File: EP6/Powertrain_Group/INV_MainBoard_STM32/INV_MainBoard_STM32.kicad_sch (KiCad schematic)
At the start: 17 parts, among them J1 FX26-30P-1SV, J10 current_DC, J2 motorSense, J9 CAN

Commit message: Inverter board adjust
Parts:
- R4: footprint Resistor_SMD:R_0402_1005Metric -> Resistor_SMD:R_0603_1608Metric
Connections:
- net GND: no longer J1.MP1, J1.MP2, J1.MP3, J1.MP4
- no-connect marks 0 -> 4
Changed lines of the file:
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@@
 	)
 	(junction
-		(at 48.26 130.81)
-		(diameter 0)
-		(color 0 0 0 0)
-	)
-	(junction
-		(at 49.53 185.42)
-		(diameter 0)
-		(color 0 0 0 0)
-	)
-	(junction
 		(at 67.31 149.86)
 		(diameter 0)
@@
 		(color 0 0 0 0)
 	)
+	(no_connect
+		(at 48.26 134.62)
+	)
+	(no_connect
+		(at 50.8 185.42)
+	)
+	(no_connect
+		(at 50.8 134.62)
+	)
+	(no_connect
+		(at 48.26 185.42)
+	)
 	(wire
 		(pts
@@
 	(wire
 		(pts
-			(xy 50.8 134.62) (xy 50.8 130.81)
-		)
-		(stroke
-			(width 0)
-			(type default)
-		)
-	)
-	(wire
-		(pts
 			(xy 31.75 157.48) (xy 35.56 157.48)
 		)
@@
 	(wire
 		(pts
-			(xy 49.53 185.42) (xy 50.8 185.42)
-		)
-		(stroke
-			(width 0)
-			(type default)
-		)
-	)
-	(wire
-		(pts
 			(xy 63.5 144.78) (xy 67.31 144.78)
 		)
@@
 	(wire
 		(pts
-			(xy 50.8 130.81) (xy 48.26 130.81)
-		)
-		(stroke
-			(width 0)
-			(type default)
-		)
-	)
-	(wire
-		(pts
 			(xy 154.94 38.1) (xy 151.13 38.1)
 		)
@@
 	(wire
 		(pts
-			(xy 49.53 187.96) (xy 49.53 185.42)
-		)
-		(stroke
-			(width 0)
-			(type default)
-		)
-	)
-	(wire
-		(pts
 			(xy 69.85 142.24) (xy 63.5 142.24)
 		)
@@
 	(wire
 		(pts
-			(xy 44.45 130.81) (xy 48.26 130.81)
-		)
-		(stroke
-			(width 0)
-			(type default)
-		)
-	)
-	(wire
-		(pts
 			(xy 64.77 152.4) (xy 64.77 154.94)
 		)
@@
 	(wire
 		(pts
-			(xy 48.26 130.81) (xy 48.26 134.62)
-		)
-		(stroke
-			(width 0)
-			(type default)
-		)
-	)
-	(wire
-		(pts
 			(xy 142.24 138.43) (xy 137.16 138.43)
 		)
@@
 	(wire
 		(pts
-			(xy 48.26 185.42) (xy 49.53 185.42)
-		)
-		(stroke
-			(width 0)
-			(type default)
-		)
-	)
-	(wire
-		(pts
 			(xy 31.75 144.78) (xy 31.75 149.86)
 		)
@@
 	(symbol
 		(lib_id "power:GND")
-		(at 44.45 130.81 0)
-		(unit 1)
-		(exclude_from_sim no)
-		(in_bom yes)
-		(on_board yes)
-		(dnp no)
-		(fields_autoplaced yes)
-		(property "Reference" "#PWR04"
-			(at 44.45 137.16 0)
-			(effects
-				(font
-					(size 1.27 1.27)
-				)
-				(hide yes)
-			)
-		)
-		(property "Value" "GND"
-			(at 44.45 135.89 0)
-			(effects
-				(font
-					(size 1.27 1.27)
-				)
-				(hide yes)
-			)
-		)
-		(property "Footprint" ""
-			(at 44.45 130.81 0)
-			(effects
-				(font
-					(size 1.27 1.27)
-				)
-				(hide yes)
-			)
-		)
-		(property "Datasheet" ""
-			(at 44.45 130.81 0)
-			(effects
-				(font
-					(size 1.27 1.27)
-				)
-				(hide yes)
-			)
-		)
-		(property "Description" "Power symbol creates a global label with name \"GND\" , ground"
-			(at 44.45 130.81 0)
-			(effects
-				(font
-					(size 1.27 1.27)
-				)
-				(hide yes)
-			)
-		)
-		(pin "1"
-		)
-		(instances
-			(project "INV_MainBoard_STM32"
-				(path "/963ad98e-e494-4953-a7e0-8b20a365a35d"
-					(reference "#PWR04")
-					(unit 1)
-				)
-			)
-		)
-	)
-	(symbol
-		(lib_id "power:GND")
 		(at 20.32 157.48 0)
 		(unit 1)
@@
 			)
 		)
-		(property "Footprint" "Resistor_SMD:R_0402_1005Metric"
+		(property "Footprint" "Resistor_SMD:R_0603_1608Metric"
 			(at 196.85 142.24 0)
 			(effects
@@
 					(unit 1)
 				)
-			)
-		)
-	)
-	(symbol
-		(lib_id "power:GND")
-		(at 49.53 187.96 0)
-		(unit 1)
-		(exclude_from_sim no)
-		(in_bom yes)
-		(on_board yes)
-		(dnp no)
-		(fields_autoplaced yes)
-		(property "Reference" "#PWR019"
-			(at 49.53 194.31 0)
-			(effects
-				(font
-					(size 1.27 1.27)
-				)
-				(hide yes)
-			)
-		)
-		(property "Value" "GND"
-			(at 49.53 193.04 0)
-			(effects
-				(font
-					(size 1.27 1.27)
-				)
-				(hide yes)
-			)
-		)
-		(property "Footprint" ""
-			(at 49.53 187.96 0)
-			(effects
-				(font
-					(size 1.27 1.27)
-				)
-				(hide yes)
-			)
-		)
-		(property "Datasheet" ""
-			(at 49.53 187.96 0)
-			(effects
-				(font
-					(size 1.27 1.27)
-				)
-				(hide yes)
-			)
-		)
-		(property "Description" "Power symbol creates a global label with name \"GND\" , ground"
-			(at 49.53 187.96 0)
-			(effects
-				(font
-					(size 1.27 1.27)
-				)
-				(hide yes)
-			)
-		)
-		(pin "1"
-		)
-		(instances
-			(project "INV_MainBoard_STM32"
-				(path "/963ad98e-e494-4953-a7e0-8b20a365a35d"
-					(reference "#PWR019")
-					(unit 1)
-				)

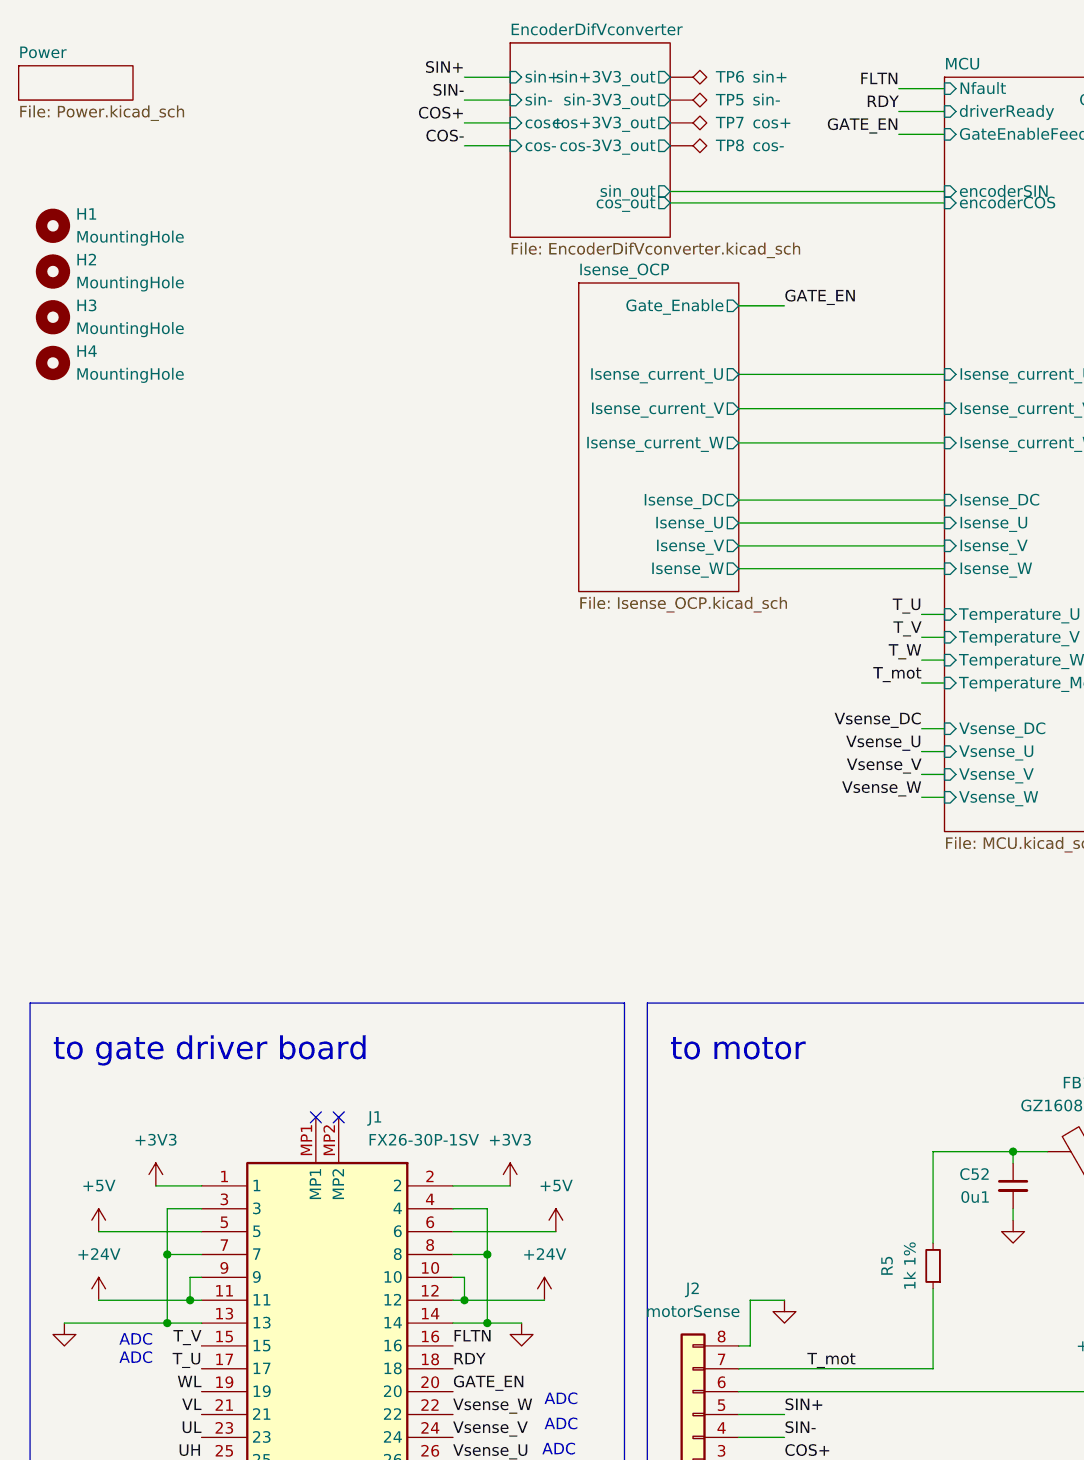
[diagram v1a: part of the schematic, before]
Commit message: batch update for JLCPCB 241117
6SBMS
ACC_HVLV1
INV_CurrentSense2
INV_CurrentSense3
DClinkCap1
INV_MainBoard_STM32
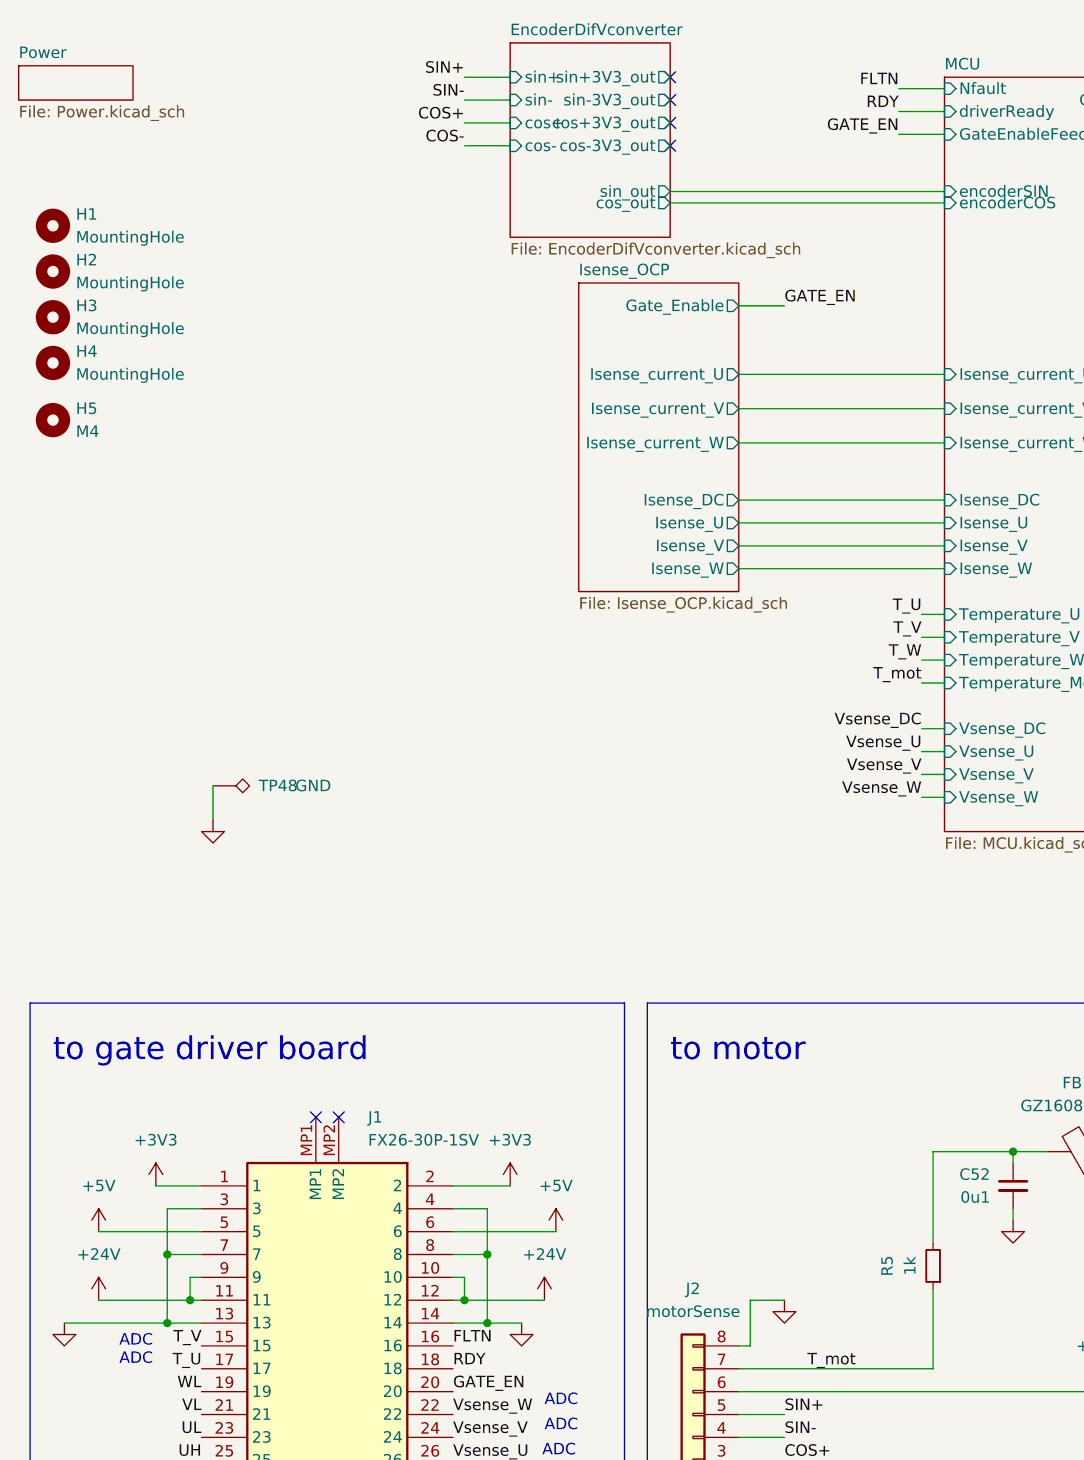
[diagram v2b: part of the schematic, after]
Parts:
- removed TP5: sin-, TestPoint:TestPoint_THTPad_D1.0mm_Drill0.5mm, symbol Connector:TestPoint_Alt
- removed TP6: sin+, TestPoint:TestPoint_THTPad_D1.0mm_Drill0.5mm, symbol Connector:TestPoint_Alt
- removed TP7: cos+, TestPoint:TestPoint_THTPad_D1.0mm_Drill0.5mm, symbol Connector:TestPoint_Alt
- removed TP8: cos-, TestPoint:TestPoint_THTPad_D1.0mm_Drill0.5mm, symbol Connector:TestPoint_Alt
- added H5: M4, MountingHole:MountingHole_4mm, symbol Mechanical:MountingHole
- added TP48: GND, TestPoint:TestPoint_THTPad_D1.0mm_Drill0.5mm, symbol Connector:TestPoint_Alt
- R5: value 1k 1% -> 1k
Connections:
- net GND: now also TP48.1
- no-connect marks 4 -> 8
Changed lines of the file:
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@@
 	(title_block
 		(title "INV_MainBoard")
-		(date "2024-11-15")
-		(rev "1")
+		(date "2024-11-16")
+		(rev "1.0")
 		(company "NTURacing Team")
 		(comment 1 "郭哲明 Jack Kuo")
@@
 	)
 	(no_connect
+		(at 87.63 26.67)
+	)
+	(no_connect
+		(at 87.63 19.05)
+	)
+	(no_connect
+		(at 87.63 24.13)
+	)
+	(no_connect
 		(at 48.26 134.62)
 	)
@@
 	)
 	(no_connect
+		(at 87.63 21.59)
+	)
+	(no_connect
 		(at 48.26 185.42)
 	)
@@
 	(wire
 		(pts
+			(xy 36.83 97.79) (xy 36.83 101.6)
+		)
+		(stroke
+			(width 0)
+			(type default)
+		)
+	)
+	(wire
+		(pts
 			(xy 115.57 86.36) (xy 118.11 86.36)
 		)
@@
 	)
 	(symbol
-		(lib_id "Connector:TestPoint_Alt")
-		(at 87.63 21.59 270)
-		(unit 1)
-		(exclude_from_sim no)
-		(in_bom yes)
-		(on_board yes)
-		(dnp no)
-		(property "Reference" "TP5"
-			(at 92.71 21.59 90)
-			(effects
-				(font
-					(size 1.27 1.27)
-				)
-				(justify left)
-			)
-		)
-		(property "Value" "sin-"
-			(at 96.774 21.59 90)
-			(effects
-				(font
-					(size 1.27 1.27)
-				)
-				(justify left)
-			)
-		)
-		(property "Footprint" "TestPoint:TestPoint_THTPad_D1.0mm_Drill0.5mm"
-			(at 87.63 26.67 0)
-			(effects
-				(font
-					(size 1.27 1.27)
-				)
-				(hide yes)
-			)
-		)
-		(property "Datasheet" "~"
-			(at 87.63 26.67 0)
-			(effects
-				(font
-					(size 1.27 1.27)
-				)
-				(hide yes)
-			)
-		)
-		(property "Description" "test point (alternative shape)"
-			(at 87.63 21.59 0)
-			(effects
-				(font
-					(size 1.27 1.27)
-				)
-				(hide yes)
-			)
-		)
-		(pin "1"
-		)
-		(instances
-			(project ""
-				(path "/963ad98e-e494-4953-a7e0-8b20a365a35d"
-					(reference "TP5")
-					(unit 1)
-				)
-			)
-		)
-	)
-	(symbol
 		(lib_id "power:+5V")
 		(at 24.13 147.32 0)
@@
 	)
 	(symbol
-		(lib_id "Connector:TestPoint_Alt")
-		(at 87.63 24.13 270)
+		(lib_id "Device:R_Small")
+		(at 116.84 151.13 180)
 		(unit 1)
 		(exclude_from_sim no)
@@
 		(on_board yes)
 		(dnp no)
-		(property "Reference" "TP7"
-			(at 92.71 24.13 90)
+		(property "Reference" "R5"
+			(at 111.76 151.13 90)
 			(effects
 				(font
 					(size 1.27 1.27)
 				)
-				(justify left)
 			)
 		)
-		(property "Value" "cos+"
-			(at 96.774 24.13 90)
+		(property "Value" "1k"
+			(at 114.3 151.13 90)
 			(effects
 				(font
 					(size 1.27 1.27)
 				)
-				(justify left)
 			)
 		)
-		(property "Footprint" "TestPoint:TestPoint_THTPad_D1.0mm_Drill0.5mm"
-			(at 87.63 29.21 0)
+		(property "Footprint" "Resistor_SMD:R_0603_1608Metric"
+			(at 116.84 151.13 0)
 			(effects
 				(font
@@
 		)
 		(property "Datasheet" "~"
-			(at 87.63 29.21 0)
+			(at 116.84 151.13 0)
 			(effects
 				(font
@@
 			)
 		)
-		(property "Description" "test point (alternative shape)"
-			(at 87.63 24.13 0)
+		(property "Description" "Resistor, small symbol"
+			(at 116.84 151.13 0)
 			(effects
 				(font
@@
 			)
 		)
+		(pin "2"
+		)
 		(pin "1"
 		)
@@
 			(project "INV_MainBoard_STM32"
 				(path "/963ad98e-e494-4953-a7e0-8b20a365a35d"
-					(reference "TP7")
+					(reference "R5")
 					(unit 1)
 				)
@@
 	)
 	(symbol
-		(lib_id "Device:R_Small")
-		(at 116.84 151.13 180)
+		(lib_id "Mechanical:MountingHole")
+		(at 19.05 57.15 0)
 		(unit 1)
-		(exclude_from_sim no)
-		(in_bom yes)
+		(exclude_from_sim yes)
+		(in_bom no)
 		(on_board yes)
 		(dnp no)
-		(property "Reference" "R5"
-			(at 111.76 151.13 90)
+		(fields_autoplaced yes)
+		(property "Reference" "H5"
+			(at 21.59 55.88 0)
 			(effects
 				(font
 					(size 1.27 1.27)
 				)
+				(justify left)
 			)
 		)
-		(property "Value" "1k 1%"
-			(at 114.3 151.13 90)
+		(property "Value" "M4"
+			(at 21.59 58.42 0)
 			(effects
 				(font
 					(size 1.27 1.27)
 				)
+				(justify left)
 			)
 		)
-		(property "Footprint" "Resistor_SMD:R_0603_1608Metric"
-			(at 116.84 151.13 0)
+		(property "Footprint" "MountingHole:MountingHole_4mm"
+			(at 19.05 57.15 0)
 			(effects
 				(font
@@
 		)
 		(property "Datasheet" "~"
-			(at 116.84 151.13 0)
+			(at 19.05 57.15 0)
 			(effects
 				(font
@@
 			)
 		)
-		(property "Description" "Resistor, small symbol"
-			(at 116.84 151.13 0)
+		(property "Description" "Mounting Hole without connection"
+			(at 19.05 57.15 0)
 			(effects
 				(font
@@
 			)
 		)
-		(pin "2"
-		)
-		(pin "1"
-		)
 		(instances
 			(project "INV_MainBoard_STM32"
 				(path "/963ad98e-e494-4953-a7e0-8b20a365a35d"
-					(reference "R5")
+					(reference "H5")
 					(unit 1)
 				)
@@
 	)
 	(symbol
+		(lib_id "Connector:TestPoint_Alt")
+		(at 36.83 97.79 270)
+		(unit 1)
+		(exclude_from_sim no)
+		(in_bom yes)
+		(on_board yes)
+		(dnp no)
+		(property "Reference" "TP48"
+			(at 41.91 97.79 90)
+			(effects
+				(font
+					(size 1.27 1.27)
+				)
+				(justify left)
+			)
+		)
+		(property "Value" "GND"
+			(at 45.974 97.79 90)
+			(effects
+				(font
+					(size 1.27 1.27)
+				)
+				(justify left)
+			)
+		)
+		(property "Footprint" "TestPoint:TestPoint_THTPad_D1.0mm_Drill0.5mm"
+			(at 36.83 102.87 0)
+			(effects
+				(font
+					(size 1.27 1.27)
+				)
+				(hide yes)
+			)
+		)
+		(property "Datasheet" "~"
+			(at 36.83 102.87 0)
+			(effects
+				(font
+					(size 1.27 1.27)
+				)
+				(hide yes)
+			)
+		)
+		(property "Description" "test point (alternative shape)"
+			(at 36.83 97.79 0)
+			(effects
+				(font
+					(size 1.27 1.27)
+				)
+				(hide yes)
+			)
+		)
+		(pin "1"
+		)
+		(instances
+			(project "INV_MainBoard_STM32"
+				(path "/963ad98e-e494-4953-a7e0-8b20a365a35d"
+					(reference "TP48")
+					(unit 1)
+				)
+			)
+		)
+	)
+	(symbol
 		(lib_id "power:GND")
 		(at 125.73 146.05 0)
@@
 	)
 	(symbol
-		(lib_id "Connector:TestPoint_Alt")
-		(at 87.63 19.05 270)
+		(lib_id "power:GND")
+		(at 36.83 101.6 0)
 		(unit 1)
 		(exclude_from_sim no)
@@
 		(on_board yes)
 		(dnp no)
-		(property "Reference" "TP6"
-			(at 92.71 19.05 90)
+		(fields_autoplaced yes)
+		(property "Reference" "#PWR04"
+			(at 36.83 107.95 0)
 			(effects
 				(font
 					(size 1.27 1.27)
 				)
-				(justify left)
+				(hide yes)
 			)
 		)
-		(property "Value" "sin+"
-			(at 96.774 19.05 90)
+		(property "Value" "GND"
+			(at 36.83 106.68 0)
 			(effects
 				(font
 					(size 1.27 1.27)
 				)
-				(justify left)
+				(hide yes)
 			)
 		)
-		(property "Footprint" "TestPoint:TestPoint_THTPad_D1.0mm_Drill0.5mm"
-			(at 87.63 24.13 0)
+		(property "Footprint" ""
+			(at 36.83 101.6 0)
 			(effects
 				(font
@@
 			)
 		)
-		(property "Datasheet" "~"
-			(at 87.63 24.13 0)
+		(property "Datasheet" ""
+			(at 36.83 101.6 0)
 			(effects
 				(font
@@
 			)
 		)
-		(property "Description" "test point (alternative shape)"
-			(at 87.63 19.05 0)
+		(property "Description" "Power symbol creates a global label with name \"GND\" , ground"
+			(at 36.83 101.6 0)
 			(effects
 				(font
@@
 			(project "INV_MainBoard_STM32"
 				(path "/963ad98e-e494-4953-a7e0-8b20a365a35d"
-					(reference "TP6")
+					(reference "#PWR04")
 					(unit 1)
 				)
@@
 					(unit 1)
 				)
-			)
-		)
-	)
-	(symbol
-		(lib_id "Connector:TestPoint_Alt")
-		(at 87.63 26.67 270)
-		(unit 1)
-		(exclude_from_sim no)
-		(in_bom yes)
-		(on_board yes)
-		(dnp no)
-		(property "Reference" "TP8"
-			(at 92.71 26.67 90)
-			(effects
-				(font
-					(size 1.27 1.27)
-				)
-				(justify left)
-			)
-		)
-		(property "Value" "cos-"
-			(at 96.774 26.67 90)
-			(effects
-				(font
-					(size 1.27 1.27)
-				)
-				(justify left)
-			)
-		)
-		(property "Footprint" "TestPoint:TestPoint_THTPad_D1.0mm_Drill0.5mm"
-			(at 87.63 31.75 0)
-			(effects
-				(font
-					(size 1.27 1.27)
-				)
-				(hide yes)
-			)
-		)
-		(property "Datasheet" "~"
-			(at 87.63 31.75 0)
-			(effects
-				(font
-					(size 1.27 1.27)
-				)
-				(hide yes)
-			)
-		)
-		(property "Description" "test point (alternative shape)"
-			(at 87.63 26.67 0)
-			(effects
-				(font
-					(size 1.27 1.27)
-				)
-				(hide yes)
-			)
-		)
-		(pin "1"
-		)
-		(instances
-			(project "INV_MainBoard_STM32"
-				(path "/963ad98e-e494-4953-a7e0-8b20a365a35d"
-					(reference "TP8")
-					(unit 1)
-				)
